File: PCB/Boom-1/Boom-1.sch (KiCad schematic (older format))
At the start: 707 parts

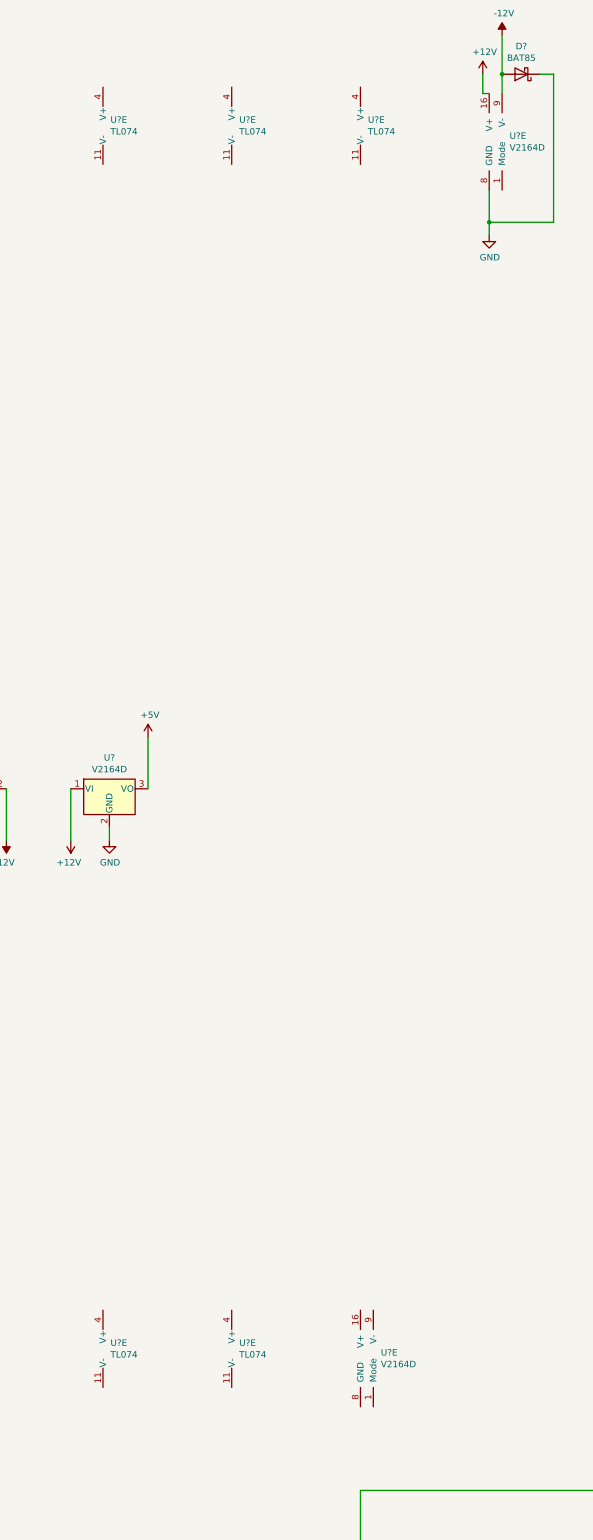
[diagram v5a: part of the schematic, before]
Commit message: added more resistor and duplicated V2164D power unit
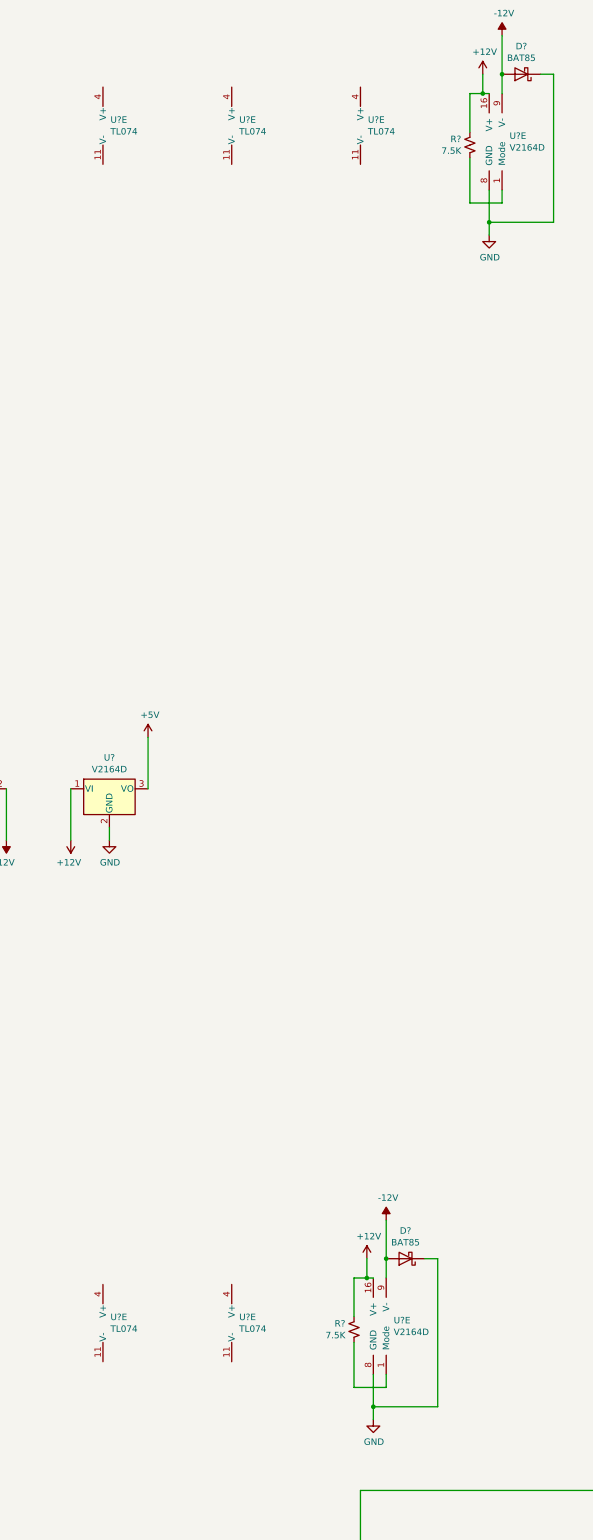
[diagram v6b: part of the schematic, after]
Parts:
- removed U?: V2164D, Package_DIP:DIP-16_W7.62mm_Socket, symbol CustomSymbols:V2164D
- added D?: BAT85, Diode_THT:D_DO-35_SOD27_P7.62mm_Horizontal, symbol Diode:BAT85
- added R? (x2): 7.5K, symbol Device:R_Small_US
- added U?: V2164D, Package_DIP:DIP-16_W7.62mm_Socket, symbol CustomSymbols:V2164D
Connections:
- net +12V: now also R?.2, R?.2, U?.16 (V+)
- net -12V: now also D?.2 (A), U?.9 (V-)
- net GND: now also D?.1 (K), U?.8 (GND)
- net at U?.1 (Mode): now also R?.1
- new net: R?.1, U?.1 (Mode)
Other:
- moved on the sheet: U?E
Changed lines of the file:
@@
 L Amplifier_Operational:TL074 U?
 U 5 1 601CF0E5
-P 3100 22800
-F 0 "U?" H 3058 22846 50  0000 L CNN
-F 1 "TL074" H 3058 22755 50  0000 L CNN
-F 2 "" H 3050 22900 50  0001 C CNN
-F 3 "http://www.ti.com/lit/ds/symlink/tl071.pdf" H 3150 23000 50  0001 C CNN
-	5    3100 22800
+P 3100 22600
+F 0 "U?" H 3058 22646 50  0000 L CNN
+F 1 "TL074" H 3058 22555 50  0000 L CNN
+F 2 "" H 3050 22700 50  0001 C CNN
+F 3 "http://www.ti.com/lit/ds/symlink/tl071.pdf" H 3150 22800 50  0001 C CNN
+	5    3100 22600
 	1    0    0    -1
 $EndComp
@@
 L Amplifier_Operational:TL074 U?
 U 5 1 601D3235
-P 4100 22800
-F 0 "U?" H 4058 22846 50  0000 L CNN
-F 1 "TL074" H 4058 22755 50  0000 L CNN
-F 2 "" H 4050 22900 50  0001 C CNN
-F 3 "http://www.ti.com/lit/ds/symlink/tl071.pdf" H 4150 23000 50  0001 C CNN
-	5    4100 22800
-	1    0    0    -1
-$EndComp
-$Comp
-L CustomSymbols:V2164D U?
-U 5 1 601DC17D
-P 5200 22850
-F 0 "U?" H 5158 22871 50  0000 L CNN
-F 1 "V2164D" H 5158 22780 50  0000 L CNN
-F 2 "Package_DIP:DIP-16_W7.62mm_Socket" H 5950 22600 50  0001 C CNN
-F 3 "" H 5250 23000 50  0001 C CNN
-	5    5200 22850
+P 4100 22600
+F 0 "U?" H 4058 22646 50  0000 L CNN
+F 1 "TL074" H 4058 22555 50  0000 L CNN
+F 2 "" H 4050 22700 50  0001 C CNN
+F 3 "http://www.ti.com/lit/ds/symlink/tl071.pdf" H 4150 22800 50  0001 C CNN
+	5    4100 22600
 	1    0    0    -1
 $EndComp
@@
 Text Notes 20700 49200 0    50   ~ 0
 Power for both envelopes
+$Comp
+L Device:R_Small_US R?
+U 1 1 600E9C81
+P 5850 13450
+F 0 "R?" H 5783 13404 50  0000 R CNN
+F 1 "7.5K" H 5783 13495 50  0000 R CNN
+F 2 "" H 5850 13450 50  0001 C CNN
+F 3 "~" H 5850 13450 50  0001 C CNN
+	1    5850 13450
+	1    0    0    1
+$EndComp
+Wire Wire Line
+	5950 13050 5850 13050
+Wire Wire Line
+	5850 13050 5850 13350
+Connection ~ 5950 13050
+Wire Wire Line
+	5850 13550 5850 13900
+Wire Wire Line
+	5850 13900 6100 13900
+Wire Wire Line
+	6100 13900 6100 13800
+$Comp
+L Diode:BAT85 D?
+U 1 1 61480CC2
+P 5350 22100
+F 0 "D?" H 5350 21883 50  0000 C CNN
+F 1 "BAT85" H 5350 21974 50  0000 C CNN
+F 2 "Diode_THT:D_DO-35_SOD27_P7.62mm_Horizontal" H 5350 21925 50  0001 C CNN
+F 3 "https://assets.nexperia.com/documents/data-sheet/BAT85.pdf" H 5350 22100 50  0001 C CNN
+	1    5350 22100
+	-1   0    0    1
+$EndComp
+Wire Wire Line
+	5200 22100 5200 22250
+$Comp
+L power:GND #PWR?
+U 1 1 61480CF9
+P 5100 23350
+F 0 "#PWR?" H 5100 23100 50  0001 C CNN
+F 1 "GND" H 5105 23177 50  0000 C CNN
+F 2 "" H 5100 23350 50  0001 C CNN
+F 3 "" H 5100 23350 50  0001 C CNN
+	1    5100 23350
+	1    0    0    -1
+$EndComp
+Wire Wire Line
+	5100 23000 5100 23250
+Wire Wire Line
+	5100 23250 5600 23250
+Wire Wire Line
+	5600 23250 5600 22100
+Wire Wire Line
+	5600 22100 5500 22100
+Connection ~ 5100 23250
+Wire Wire Line
+	5100 23250 5100 23350
+$Comp
+L power:-12V #PWR?
+U 1 1 61480D11
+P 5200 21800
+F 0 "#PWR?" H 5200 21900 50  0001 C CNN
+F 1 "-12V" H 5215 21973 50  0000 C CNN
+F 2 "" H 5200 21800 50  0001 C CNN
+F 3 "" H 5200 21800 50  0001 C CNN
+	1    5200 21800
+	1    0    0    -1
+$EndComp
+Wire Wire Line
+	5200 21800 5200 22100
+Connection ~ 5200 22100
+$Comp
+L power:+12V #PWR?
+U 1 1 61480D25
+P 5050 22100
+F 0 "#PWR?" H 5050 21950 50  0001 C CNN
+F 1 "+12V" H 5065 22273 50  0000 C CNN
+F 2 "" H 5050 22100 50  0001 C CNN
+F 3 "" H 5050 22100 50  0001 C CNN
+	1    5050 22100
+	1    0    0    -1
+$EndComp
+Wire Wire Line
+	5050 22100 5050 22250
+Wire Wire Line
+	5050 22250 5100 22250
+$Comp
+L CustomSymbols:V2164D U?
+U 5 1 61480D3D
+P 5300 22600
+F 0 "U?" H 5258 22621 50  0000 L CNN
+F 1 "V2164D" H 5258 22530 50  0000 L CNN
+F 2 "Package_DIP:DIP-16_W7.62mm_Socket" H 6050 22350 50  0001 C CNN
+F 3 "" H 5350 22750 50  0001 C CNN
+	5    5300 22600
+	1    0    0    -1
+$EndComp
+$Comp
+L Device:R_Small_US R?
+U 1 1 61480D7D
+P 4950 22650
+F 0 "R?" H 4883 22604 50  0000 R CNN
+F 1 "7.5K" H 4883 22695 50  0000 R CNN
+F 2 "" H 4950 22650 50  0001 C CNN
+F 3 "~" H 4950 22650 50  0001 C CNN
+	1    4950 22650
+	1    0    0    1
+$EndComp
+Wire Wire Line
+	5050 22250 4950 22250
+Wire Wire Line
+	4950 22250 4950 22550
+Connection ~ 5050 22250
+Wire Wire Line
+	4950 22750 4950 23100
+Wire Wire Line
+	4950 23100 5200 23100
+Wire Wire Line
+	5200 23100 5200 23000
 $EndSCHEMATC

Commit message: Moved amp power units and added V2164D power unit
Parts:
- added D?: BAT85, Diode_THT:D_DO-35_SOD27_P7.62mm_Horizontal, symbol Diode:BAT85
- added R?: 7.5K, symbol Device:R_Small_US
- added U?: V2164D, Package_DIP:DIP-16_W7.62mm_Socket, symbol CustomSymbols:V2164D
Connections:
- net +12V: now also R?.2, U?.16 (V+)
- net -12V: now also D?.2 (A), U?.9 (V-)
- net GND: now also D?.1 (K), U?.8 (GND)
- new net: R?.1, U?.1 (Mode)
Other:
- moved on the sheet: U?C, U?E
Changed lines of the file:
@@
 L Amplifier_Operational:TL074 U?
 U 5 1 6014D7EE
-P 30100 18300
-F 0 "U?" H 30058 18346 50  0000 L CNN
-F 1 "TL074" H 30058 18255 50  0000 L CNN
-F 2 "" H 30050 18400 50  0001 C CNN
-F 3 "http://www.ti.com/lit/ds/symlink/tl071.pdf" H 30150 18500 50  0001 C CNN
-	5    30100 18300
+P 29050 28050
+F 0 "U?" H 29008 28096 50  0000 L CNN
+F 1 "TL074" H 29008 28005 50  0000 L CNN
+F 2 "" H 29000 28150 50  0001 C CNN
+F 3 "http://www.ti.com/lit/ds/symlink/tl071.pdf" H 29100 28250 50  0001 C CNN
+	5    29050 28050
 	1    0    0    -1
 $EndComp
@@
 L Amplifier_Operational:TL074 U?
 U 5 1 6015593F
-P 31100 18300
-F 0 "U?" H 31058 18346 50  0000 L CNN
-F 1 "TL074" H 31058 18255 50  0000 L CNN
-F 2 "" H 31050 18400 50  0001 C CNN
-F 3 "http://www.ti.com/lit/ds/symlink/tl071.pdf" H 31150 18500 50  0001 C CNN
-	5    31100 18300
+P 30050 28050
+F 0 "U?" H 30008 28096 50  0000 L CNN
+F 1 "TL074" H 30008 28005 50  0000 L CNN
+F 2 "" H 30000 28150 50  0001 C CNN
+F 3 "http://www.ti.com/lit/ds/symlink/tl071.pdf" H 30100 28250 50  0001 C CNN
+	5    30050 28050
 	1    0    0    -1
 $EndComp
@@
 L Amplifier_Operational:TL074 U?
 U 5 1 601576BC
-P 32100 18300
-F 0 "U?" H 32058 18346 50  0000 L CNN
-F 1 "TL074" H 32058 18255 50  0000 L CNN
-F 2 "" H 32050 18400 50  0001 C CNN
-F 3 "http://www.ti.com/lit/ds/symlink/tl071.pdf" H 32150 18500 50  0001 C CNN
-	5    32100 18300
+P 31050 28050
+F 0 "U?" H 31008 28096 50  0000 L CNN
+F 1 "TL074" H 31008 28005 50  0000 L CNN
+F 2 "" H 31000 28150 50  0001 C CNN
+F 3 "http://www.ti.com/lit/ds/symlink/tl071.pdf" H 31100 28250 50  0001 C CNN
+	5    31050 28050
 	1    0    0    -1
 $EndComp
@@
 L Amplifier_Operational:TL072 U?
 U 3 1 601601BA
-P 33100 18300
-F 0 "U?" H 33058 18346 50  0000 L CNN
-F 1 "TL072" H 33058 18255 50  0000 L CNN
-F 2 "" H 33100 18300 50  0001 C CNN
-F 3 "http://www.ti.com/lit/ds/symlink/tl071.pdf" H 33100 18300 50  0001 C CNN
-	3    33100 18300
+P 32050 28050
+F 0 "U?" H 32008 28096 50  0000 L CNN
+F 1 "TL072" H 32008 28005 50  0000 L CNN
+F 2 "" H 32050 28050 50  0001 C CNN
+F 3 "http://www.ti.com/lit/ds/symlink/tl071.pdf" H 32050 28050 50  0001 C CNN
+	3    32050 28050
 	1    0    0    -1
 $EndComp
@@
 L Amplifier_Operational:TL074 U?
 U 5 1 69EDED55
-P 30100 42300
-F 0 "U?" H 30058 42346 50  0000 L CNN
-F 1 "TL074" H 30058 42255 50  0000 L CNN
-F 2 "" H 30050 42400 50  0001 C CNN
-F 3 "http://www.ti.com/lit/ds/symlink/tl071.pdf" H 30150 42500 50  0001 C CNN
-	5    30100 42300
+P 29550 32950
+F 0 "U?" H 29508 32996 50  0000 L CNN
+F 1 "TL074" H 29508 32905 50  0000 L CNN
+F 2 "" H 29500 33050 50  0001 C CNN
+F 3 "http://www.ti.com/lit/ds/symlink/tl071.pdf" H 29600 33150 50  0001 C CNN
+	5    29550 32950
 	1    0    0    -1
 $EndComp
@@
 L Amplifier_Operational:TL074 U?
 U 5 1 69EE8A55
-P 31100 42300
-F 0 "U?" H 31058 42346 50  0000 L CNN
-F 1 "TL074" H 31058 42255 50  0000 L CNN
-F 2 "" H 31050 42400 50  0001 C CNN
-F 3 "http://www.ti.com/lit/ds/symlink/tl071.pdf" H 31150 42500 50  0001 C CNN
-	5    31100 42300
+P 30550 32950
+F 0 "U?" H 30508 32996 50  0000 L CNN
+F 1 "TL074" H 30508 32905 50  0000 L CNN
+F 2 "" H 30500 33050 50  0001 C CNN
+F 3 "http://www.ti.com/lit/ds/symlink/tl071.pdf" H 30600 33150 50  0001 C CNN
+	5    30550 32950
 	1    0    0    -1
 $EndComp
@@
 L Amplifier_Operational:TL072 U?
 U 3 1 69EF1098
-P 32100 42300
-F 0 "U?" H 32058 42346 50  0000 L CNN
-F 1 "TL072" H 32058 42255 50  0000 L CNN
-F 2 "" H 32100 42300 50  0001 C CNN
-F 3 "http://www.ti.com/lit/ds/symlink/tl071.pdf" H 32100 42300 50  0001 C CNN
-	3    32100 42300
+P 31550 32950
+F 0 "U?" H 31508 32996 50  0000 L CNN
+F 1 "TL072" H 31508 32905 50  0000 L CNN
+F 2 "" H 31550 32950 50  0001 C CNN
+F 3 "http://www.ti.com/lit/ds/symlink/tl071.pdf" H 31550 32950 50  0001 C CNN
+	3    31550 32950
 	1    0    0    -1
 $EndComp
@@
 Wire Wire Line
 	5200 23100 5200 23000
+$Comp
+L Diode:BAT85 D?
+U 1 1 685BE66A
+P 30700 29900
+F 0 "D?" H 30700 29683 50  0000 C CNN
+F 1 "BAT85" H 30700 29774 50  0000 C CNN
+F 2 "Diode_THT:D_DO-35_SOD27_P7.62mm_Horizontal" H 30700 29725 50  0001 C CNN
+F 3 "https://assets.nexperia.com/documents/data-sheet/BAT85.pdf" H 30700 29900 50  0001 C CNN
+	1    30700 29900
+	-1   0    0    1
+$EndComp
+Wire Wire Line
+	30550 29900 30550 30050
+$Comp
+L power:GND #PWR?
+U 1 1 685BE6A1
+P 30450 31150
+F 0 "#PWR?" H 30450 30900 50  0001 C CNN
+F 1 "GND" H 30455 30977 50  0000 C CNN
+F 2 "" H 30450 31150 50  0001 C CNN
+F 3 "" H 30450 31150 50  0001 C CNN
+	1    30450 31150
+	1    0    0    -1
+$EndComp
+Wire Wire Line
+	30450 30800 30450 31050
+Wire Wire Line
+	30450 31050 30950 31050
+Wire Wire Line
+	30950 31050 30950 29900
+Wire Wire Line
+	30950 29900 30850 29900
+Connection ~ 30450 31050
+Wire Wire Line
+	30450 31050 30450 31150
+$Comp
+L power:-12V #PWR?
+U 1 1 685BE6B9
+P 30550 29600
+F 0 "#PWR?" H 30550 29700 50  0001 C CNN
+F 1 "-12V" H 30565 29773 50  0000 C CNN
+F 2 "" H 30550 29600 50  0001 C CNN
+F 3 "" H 30550 29600 50  0001 C CNN
+	1    30550 29600
+	1    0    0    -1
+$EndComp
+Wire Wire Line
+	30550 29600 30550 29900
+Connection ~ 30550 29900
+$Comp
+L power:+12V #PWR?
+U 1 1 685BE6CD
+P 30400 29900
+F 0 "#PWR?" H 30400 29750 50  0001 C CNN
+F 1 "+12V" H 30415 30073 50  0000 C CNN
+F 2 "" H 30400 29900 50  0001 C CNN
+F 3 "" H 30400 29900 50  0001 C CNN
+	1    30400 29900
+	1    0    0    -1
+$EndComp
+Wire Wire Line
+	30400 29900 30400 30050
+Wire Wire Line
+	30400 30050 30450 30050
+$Comp
+L CustomSymbols:V2164D U?
+U 5 1 685BE6E5
+P 30650 30400
+F 0 "U?" H 30608 30421 50  0000 L CNN
+F 1 "V2164D" H 30608 30330 50  0000 L CNN
+F 2 "Package_DIP:DIP-16_W7.62mm_Socket" H 31400 30150 50  0001 C CNN
+F 3 "" H 30700 30550 50  0001 C CNN
+	5    30650 30400
+	1    0    0    -1
+$EndComp
+$Comp
+L Device:R_Small_US R?
+U 1 1 685BE725
+P 30300 30450
+F 0 "R?" H 30233 30404 50  0000 R CNN
+F 1 "7.5K" H 30233 30495 50  0000 R CNN
+F 2 "" H 30300 30450 50  0001 C CNN
+F 3 "~" H 30300 30450 50  0001 C CNN
+	1    30300 30450
+	1    0    0    1
+$EndComp
+Wire Wire Line
+	30400 30050 30300 30050
+Wire Wire Line
+	30300 30050 30300 30350
+Connection ~ 30400 30050
+Wire Wire Line
+	30300 30550 30300 30900
+Wire Wire Line
+	30300 30900 30550 30900
+Wire Wire Line
+	30550 30900 30550 30800
 $EndSCHEMATC

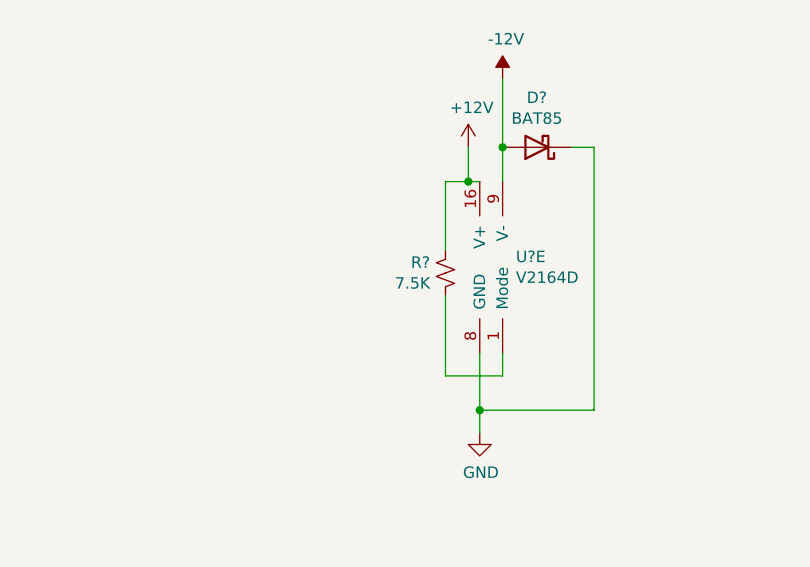
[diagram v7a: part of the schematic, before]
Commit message: linearized v2164d mode
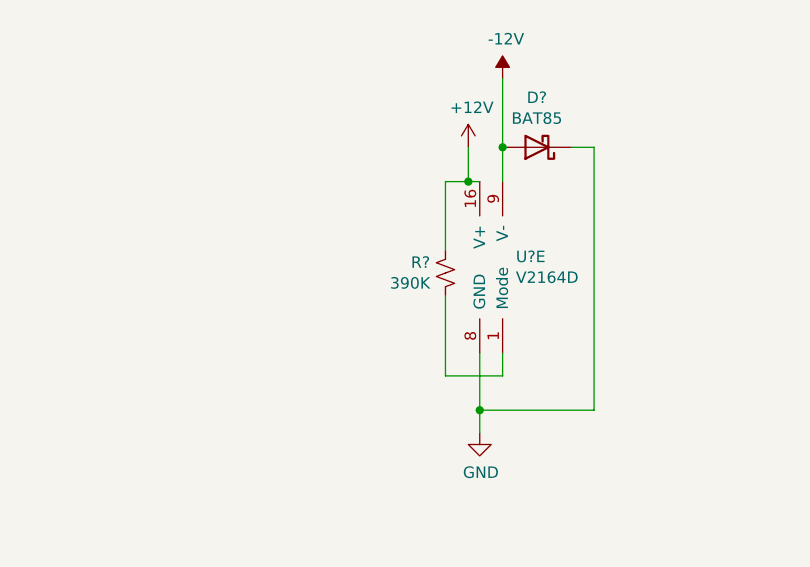
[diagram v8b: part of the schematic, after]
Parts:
- R?: value 7.5K -> 390K
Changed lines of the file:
@@
 P 30300 30450
 F 0 "R?" H 30233 30404 50  0000 R CNN
-F 1 "7.5K" H 30233 30495 50  0000 R CNN
+F 1 "390K" H 30233 30495 50  0000 R CNN
 F 2 "" H 30300 30450 50  0001 C CNN
 F 3 "~" H 30300 30450 50  0001 C CNN
